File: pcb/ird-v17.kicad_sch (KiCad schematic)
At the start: 21 parts, among them J1 AVR-TPI-6, J2 Conn_02x06_Odd_Even, K1 G6K-2, Q1 NPN 10K, U1 ATtiny20-U, U2 TSOP75438TT, U3 TLVM365R15RDNR

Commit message: Rearrange pins
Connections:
- net TPIDATA: no longer R3.1
- net DI_SENSE: now reaches U1.B2 (PA6)
- net DI_SENSE: now also U2.3 (~{OUT})
- net ADC2_DELAY renamed AI_DELAY
- net AI_DELAY: now also U1.C1 (PA5); no longer U1.A3 (PA1)
- net OC0A_LED renamed PWMO_LED
- removed net PA4_SENSE: U1.C1 (PA5), U2.3 (~{OUT})
- net PA5_RELAY renamed DO_RELAY
- new net DO_LED: R3.1, U1.A3 (PA1)

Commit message: PCB update
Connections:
- net DO_RELAY: now also Q1.2 (B1); no longer Q1.5 (B2)
- net PWMO_LED: now also Q1.5 (B2); no longer Q1.2 (B1)
- net at D3.2 (A), K1.8: now also Q1.6 (C1); no longer Q1.3 (C2)
- net at R2.2: now also Q1.3 (C2); no longer Q1.6 (C1)

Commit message: Update BOM
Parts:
- C1: $/1 (none) -> $0.33; $/10 (none) -> $1.98
- C2, C5: $/1 (none) -> $0.10; $/10 (none) -> $0.31
- C3: $/1 (none) -> $0.23; $/10 (none) -> $1.31
- C4: $/1 (none) -> $0.17; $/10 (none) -> $0.99
- C6: $/1 (none) -> $0.61; $/10 (none) -> $6.01
- D1: value D_Bridge_-AA+ -> CD-HD2006L; $/1 (none) -> $0.98; $/10 (none) -> $7.33
- D2: $/1 (none) -> $0.65; $/10 (none) -> $4.52
- D3: $/1 (none) -> $0.13; $/10 (none) -> $0.92
- D4: $/1 (none) -> $0.44; $/10 (none) -> $2.99; Optional (none) -> TRUE
- J2: $/1 (none) -> $0.81; $/10 (none) -> $6.86
- K1: $/1 (none) -> $4.30; $/10 (none) -> $38.28
- Q1: value NPN 10K -> MUN5211DW1T1G; $/1 (none) -> $0.23; $/10 (none) -> $1.39
- R1: $/1 (none) -> $0.11; $/10 (none) -> $0.52
- R2: $/1 (none) -> $0.12; $/10 (none) -> $0.54
- R3: $/1 (none) -> $0.11; $/10 (none) -> $0.53; Optional (none) -> TRUE
- U1: value ATtiny20-U -> ATtiny20-UUR; $/1 (none) -> $1.18; $/10 (none) -> $11.80
- U2: $/1 (none) -> $1.34; $/10 (none) -> $11.22
- U3: $/1 (none) -> $2.40; $/10 (none) -> $17.79
- VR1: $/1 (none) -> $0.45; $/10 (none) -> $3.79

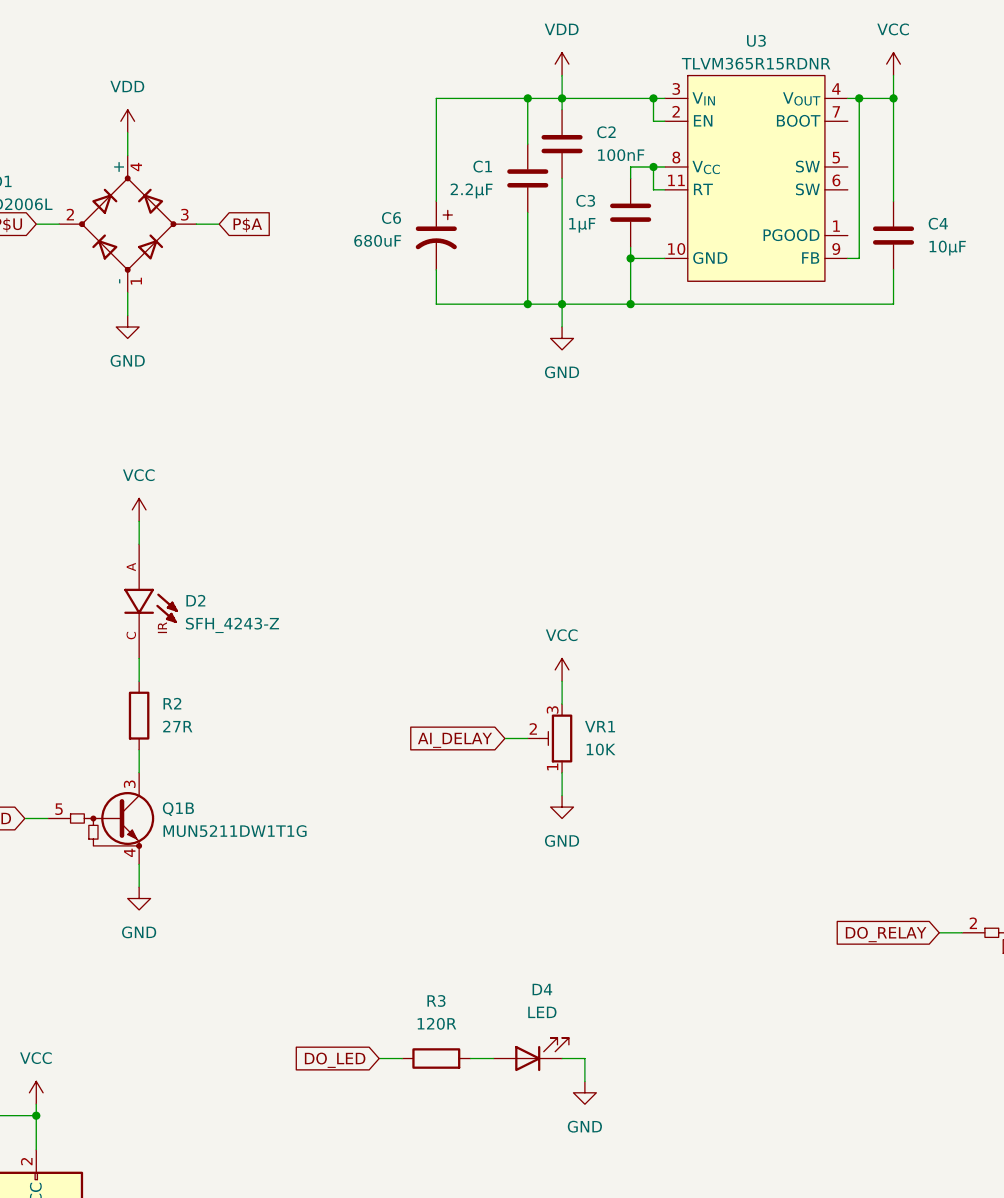
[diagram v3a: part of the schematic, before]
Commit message: Update to use 5V for consistent ATTINY20 programming
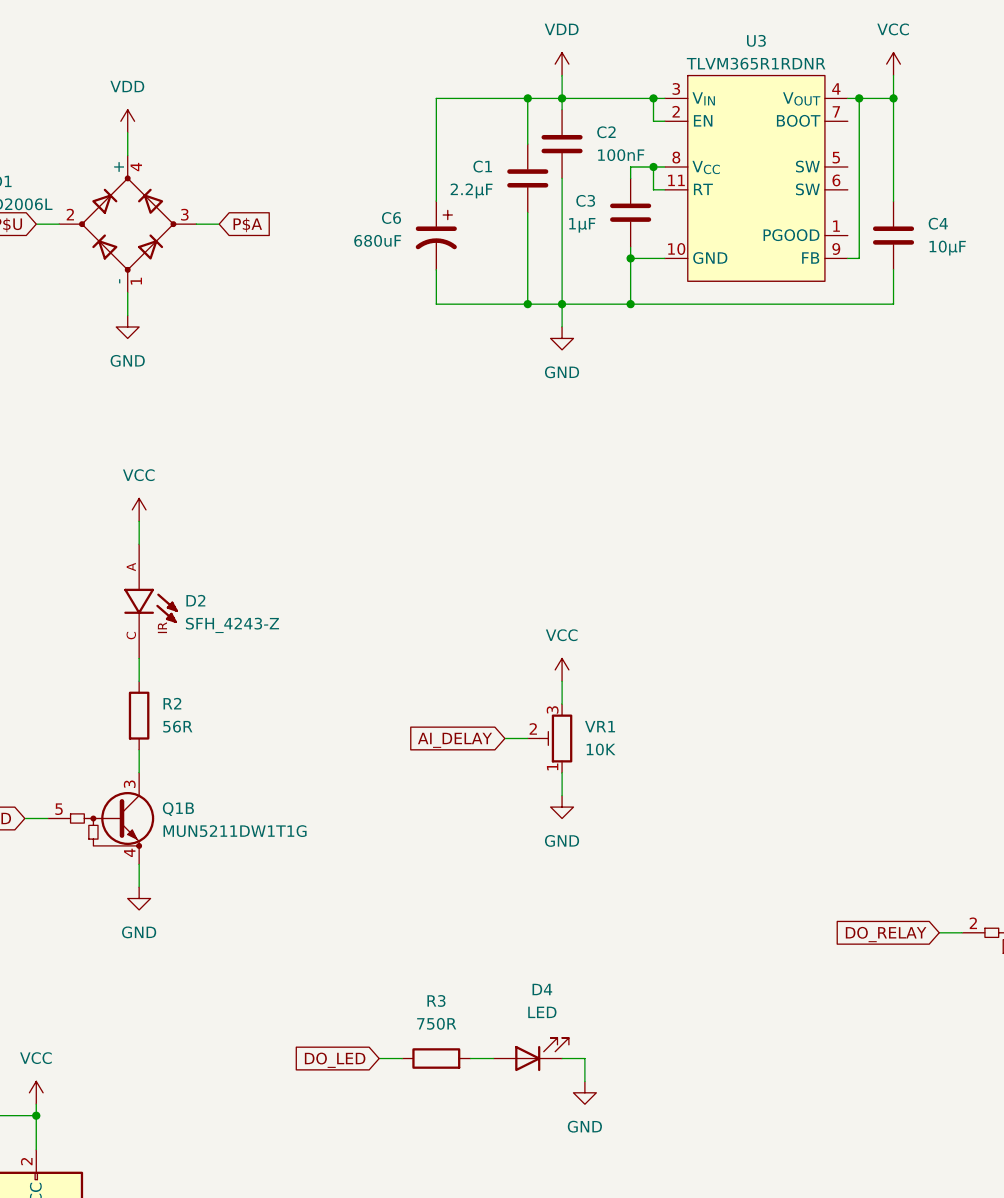
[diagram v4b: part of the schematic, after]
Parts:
- K1: $/10 $38.28 -> $40.57
- R2: value 27R -> 56R
- R3: value 120R -> 750R
- U3: value TLVM365R15RDNR -> TLVM365R1RDNR
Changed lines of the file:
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@@
 			)
 		)
-		(property "Value" "120R"
+		(property "Value" "750R"
 			(at 146.05 133.35 90)
 			(effects
@@
 			)
 		)
-		(property "Description" "RCS0402120RFKED"
+		(property "Description" "RCS0402750RFKED"
 			(at 146.05 137.16 0)
 			(effects
@@
 			)
 		)
-		(property "Description" "TC42X-2-10E"
+		(property "Description" "TC42X-2-103E"
 			(at 160.02 101.6 0)
 			(effects
@@
 			)
 		)
-		(property "Description" "G6K-2G-Y-TR DC3"
+		(property "Description" "G6K-2G-Y-TR DC5"
 			(at 245.11 105.41 0)
 			(effects
@@
 			)
 		)
-		(property "$/10" "$38.28"
+		(property "$/10" "$40.57"
 			(at 245.11 105.41 0)
 			(effects
@@
 			)
 		)
-		(property "Value" "TLVM365R15RDNR"
+		(property "Value" "TLVM365R1RDNR"
 			(at 181.61 26.67 0)
 			(effects
@@
 			)
 		)
-		(property "Description" "TLVM365R15RDNR"
+		(property "Description" "TLVM365R1RDNR"
 			(at 181.61 45.72 0)
 			(effects
@@
 			)
 		)
-		(property "Value" "27R"
+		(property "Value" "56R"
 			(at 115.57 100.3299 0)
 			(effects
@@
 			)
 		)
-		(property "Description" "RCS040227R0FKED"
+		(property "Description" "RCS040256R0FKED"
 			(at 113.03 99.06 0)
 			(effects
